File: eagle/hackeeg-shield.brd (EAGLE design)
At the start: 101.6 x 53.3 mm, 144 parts, among them IC1 ADS1299IPAG, IC10 TXB0108PWR, IC11 TXB0108PWR, IC2 TPS72325DBVT, IC3 TPS73225DBVT, IC5 24AA256UID, IC6 TPS60403DBVT, IC7 OPA376DBV, IC8 OPA376DBV, IC9 TXS0102DCUR

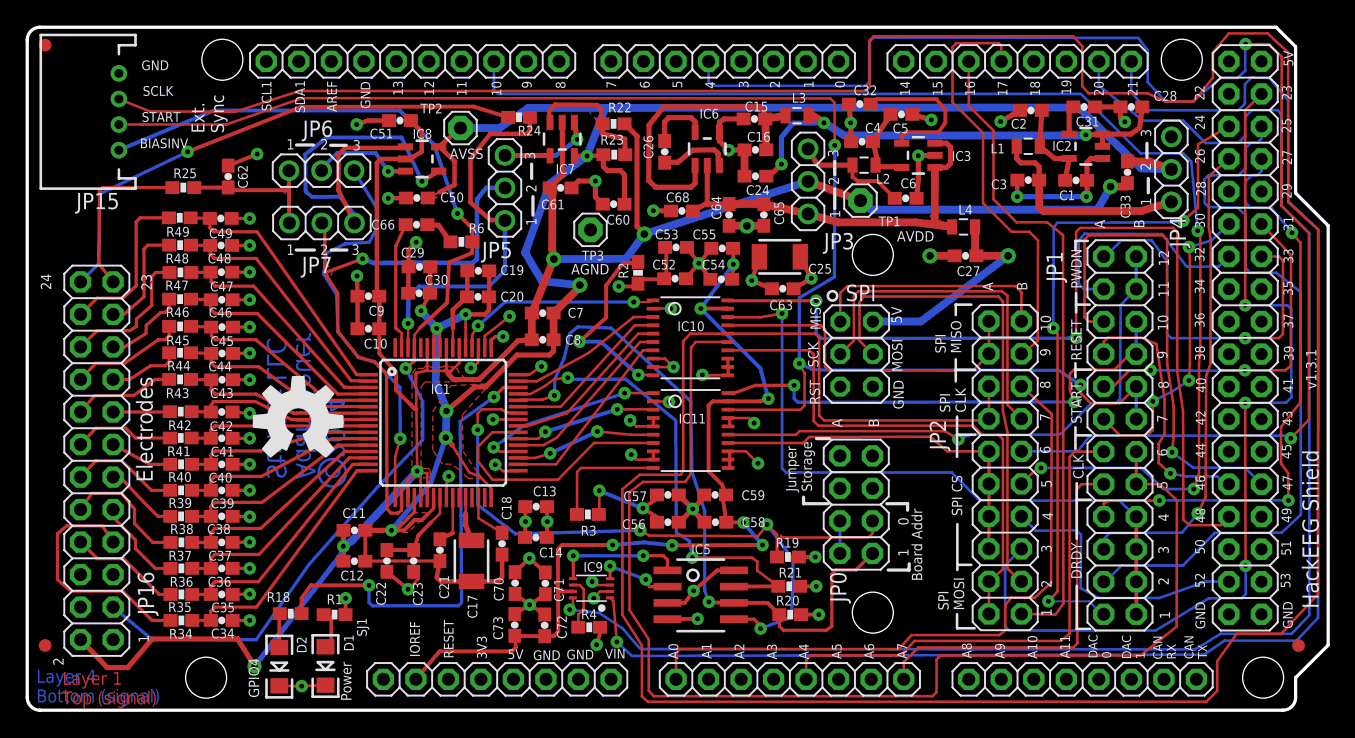
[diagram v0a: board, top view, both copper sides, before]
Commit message: fixed schematic and board bug - opamp OPA376 VDD and VSS pins were reversed; updated schematic and board version to 1.3.1
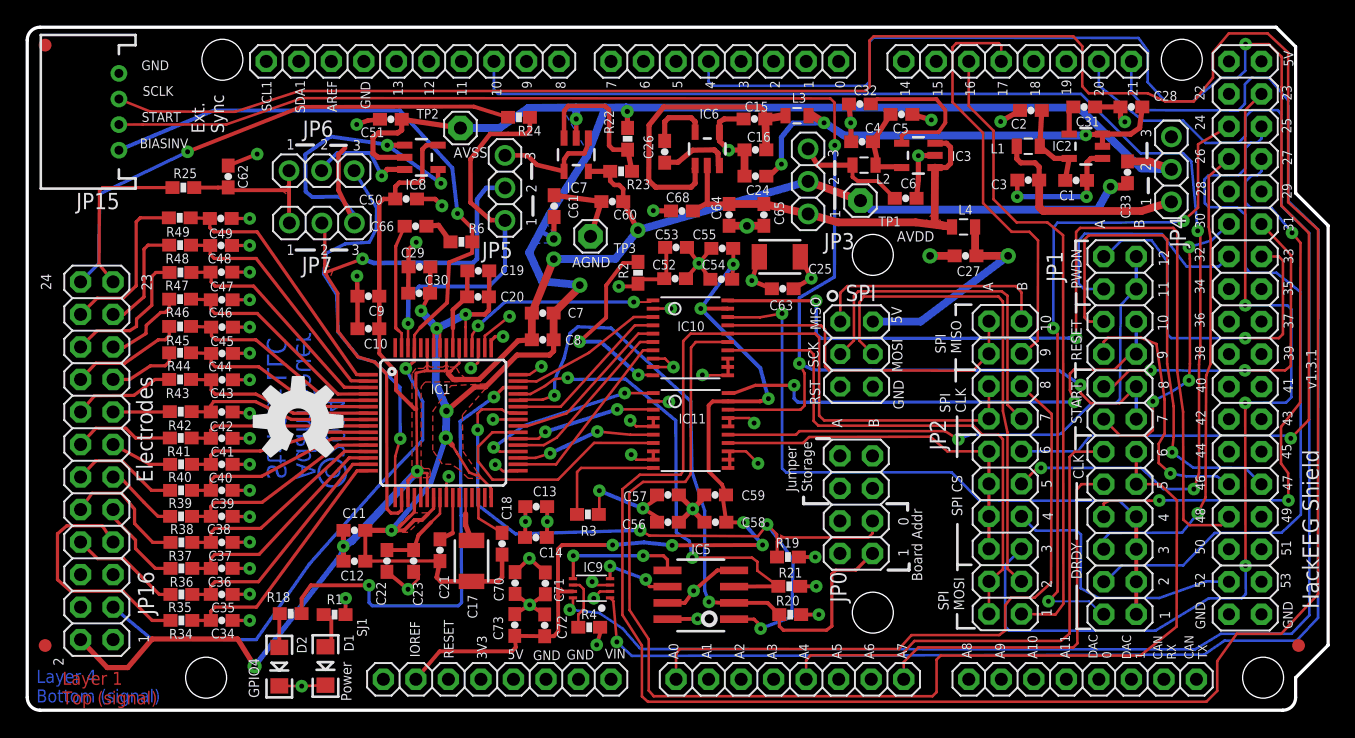
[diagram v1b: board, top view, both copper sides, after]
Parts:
- moved IC7 1.64 mm to (43.0, 43.5)
- moved R22 1.60 mm to (47.0, 44.8), turned to 90 degrees
- moved C61 1.51 mm to (41.3, 39.5), turned to 270 degrees
- moved R23 1.40 mm to (46.5, 42.2)
- moved C50 0.84 mm to (29.7, 40.1), turned to 0 degrees
- moved C51 0.72 mm to (28.5, 46.3)
- moved TP3 0.51 mm to (44.1, 37.1)
- moved C60 0.23 mm to (45.8, 39.9)
- moved C66 0.15 mm to (30.5, 37.9)
- moved IC8 0.14 mm to (30.9, 43.3)
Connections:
- net AVDD: now also C50.1, C60.1, IC7.5, IC8.5, R23.1; no longer C51.2, C61.2, IC7.2, IC8.2, R22.2
- net AVSS: now also C51.2, C61.2, IC7.2, IC8.2, R22.2; no longer C50.1, C60.1, IC7.5, IC8.5, R23.1
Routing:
- net AVDD: track 175.6 -> 160.1 mm
- net N$17: track 32.7 -> 29.2 mm, vias 1 -> 2
- net DVDD: track 42.1 -> 39.5 mm
- net AGND: track 152.4 -> 154.6 mm, vias 56 -> 55
- net N$18: track 10.9 -> 9.01 mm, vias 1 -> 0
- net N$15: track 10.3 -> 12.0 mm
- net AVSS: track 183.1 -> 184.1 mm, vias 8 -> 10
- net N$16: track 7.95 -> 8.49 mm

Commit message: improved AVSS trace width on bottom layer; removed trace running through the middle of caps; improved text sizes for configuration labels
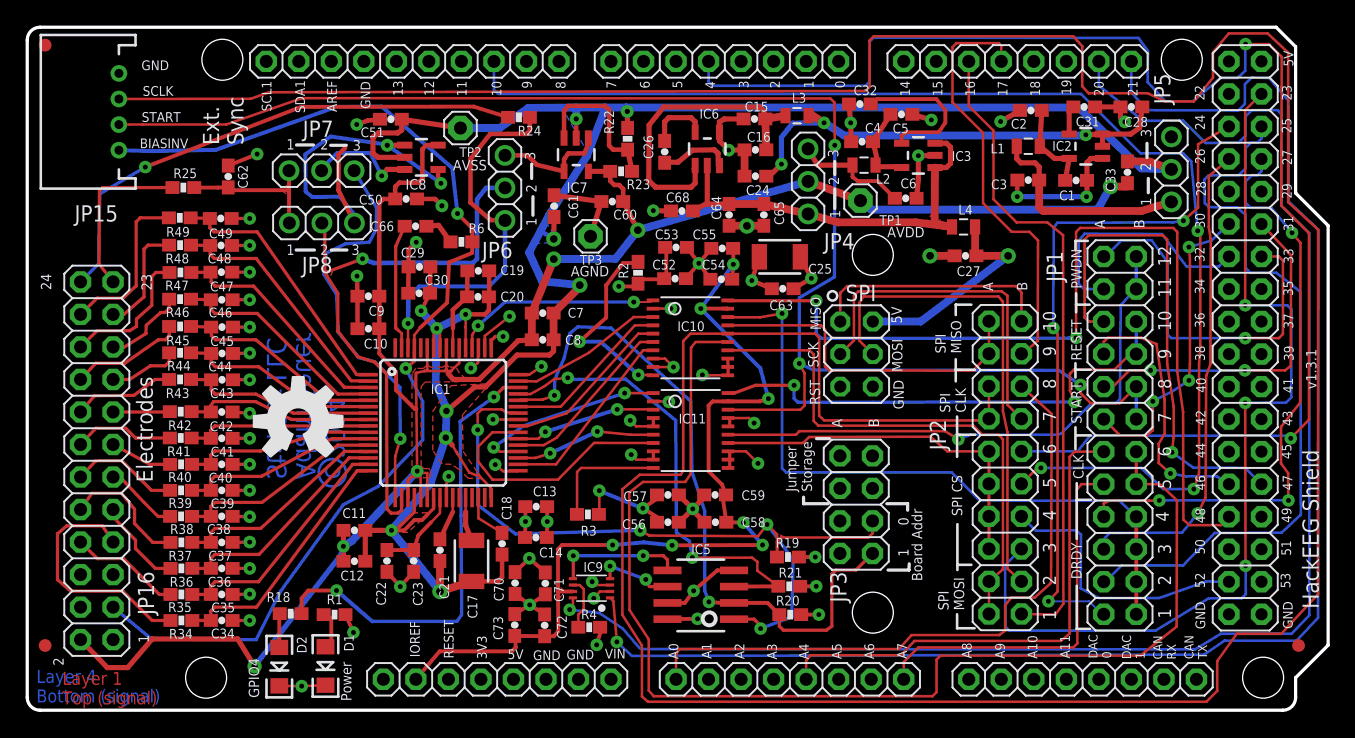
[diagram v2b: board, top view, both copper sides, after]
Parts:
- removed JP0: BOARD_ADDRESS, headers:2X04
- added JP20: PWMH, SmartPrj:1X10
- JP3: value 5V-2.5V -> BOARD_ADDRESS; device headers:1X03 -> headers:2X04
- JP4: value -2.5V-GND -> 5V-2.5V
- JP5: value SRB1-BIAS -> -2.5V-GND; device adafruit:1X03 -> headers:1X03
- JP6: value SRB2-REF_ELEC -> SRB1-BIAS
- JP7: value SRB1-REF_ELEC -> SRB2-REF_ELEC
- JP8: value PWMH -> SRB1-REF_ELEC; device SmartPrj:1X10 -> adafruit:1X03
- moved JP5 52.1 mm to (89.5, 42.4)
- moved JP4 28.4 mm to (61.1, 41.4)
- moved JP3 25.5 mm to (64.9, 16.2)
- moved JP8 14.5 mm to (23.1, 38.2)
- moved JP6 14.4 mm to (37.4, 40.9), turned to 90 degrees
- moved JP7 4.09 mm to (23.1, 42.3)
- renumbered JP10 to JP22, JP11 to JP23, JP12 to JP24, JP13 to JP25, JP14 to JP26, JP9 to JP21
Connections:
- net !ADC_CS_1: now also JP20.8; no longer JP8.8
- net +2.5V: now also JP4.3; no longer JP3.3
- net -2.5V: now also JP5.1; no longer JP4.1
- net AGND: now also JP5.3; no longer JP4.3
- net AVDD: now also JP4.2; no longer JP3.2
- net AVSS: now also JP5.2; no longer JP4.2
- net BIAS_ELEC: now also JP6.1; no longer JP5.1
- net BOARD_ADDR_0: now also JP3.3; no longer JP0.3
- net BOARD_ADDR_1: now also JP3.1; no longer JP0.1
- net DVDD: now also JP3.2, JP3.4; no longer JP0.2, JP0.4
- net N$16: now also JP7.2; no longer JP6.2
- net N$17: now also JP8.3; no longer JP7.3
- net N$18: now also JP6.3; no longer JP5.3
- net N$27: now also JP20.3; no longer JP8.3
- net N$28: now also JP20.4; no longer JP8.4
- net N$29: now also JP20.5; no longer JP8.5
- net N$30: now also JP20.6; no longer JP8.6
- net N$31: now also JP20.7; no longer JP8.7
- net N$33: now also JP20.10; no longer JP8.10
- net N$6: now also JP20.9; no longer JP8.9
- net N$6001: now also JP20.2; no longer JP8.2
- net N$6002: now also JP20.1; no longer JP8.1
- net REF_ELEC: now also JP8.1; no longer JP6.1
- net SRB1: now also JP6.2, JP8.2; no longer JP5.2, JP7.2
- net SRB2: now also JP7.3; no longer JP6.3
- net VCC_5V_FILTERED: now also JP4.1; no longer JP3.1
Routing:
- net AVSS: track 184.1 -> 185.2 mm, vias 10 -> 11
- net AGND: track 154.6 -> 153.7 mm
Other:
- board text removed: "SJ1"

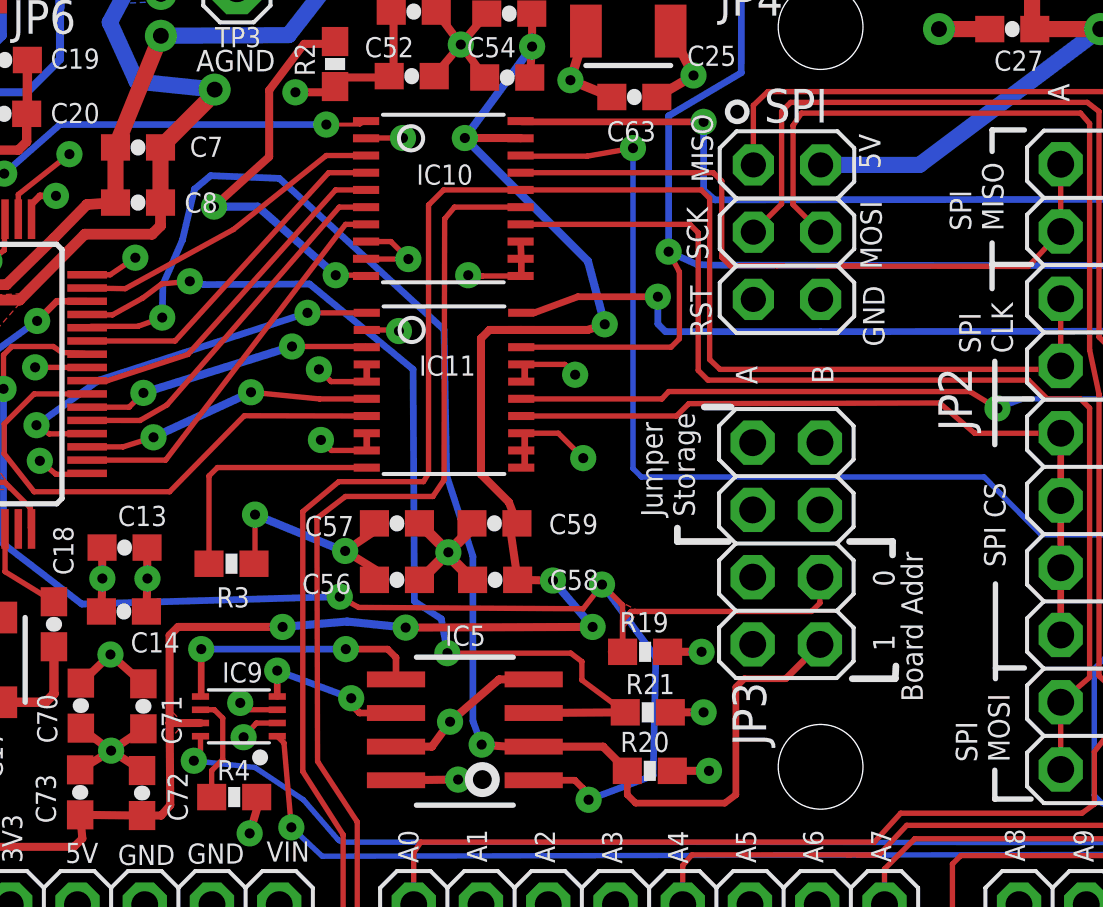
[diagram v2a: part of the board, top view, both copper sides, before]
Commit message: improved trace routing on bottom layer
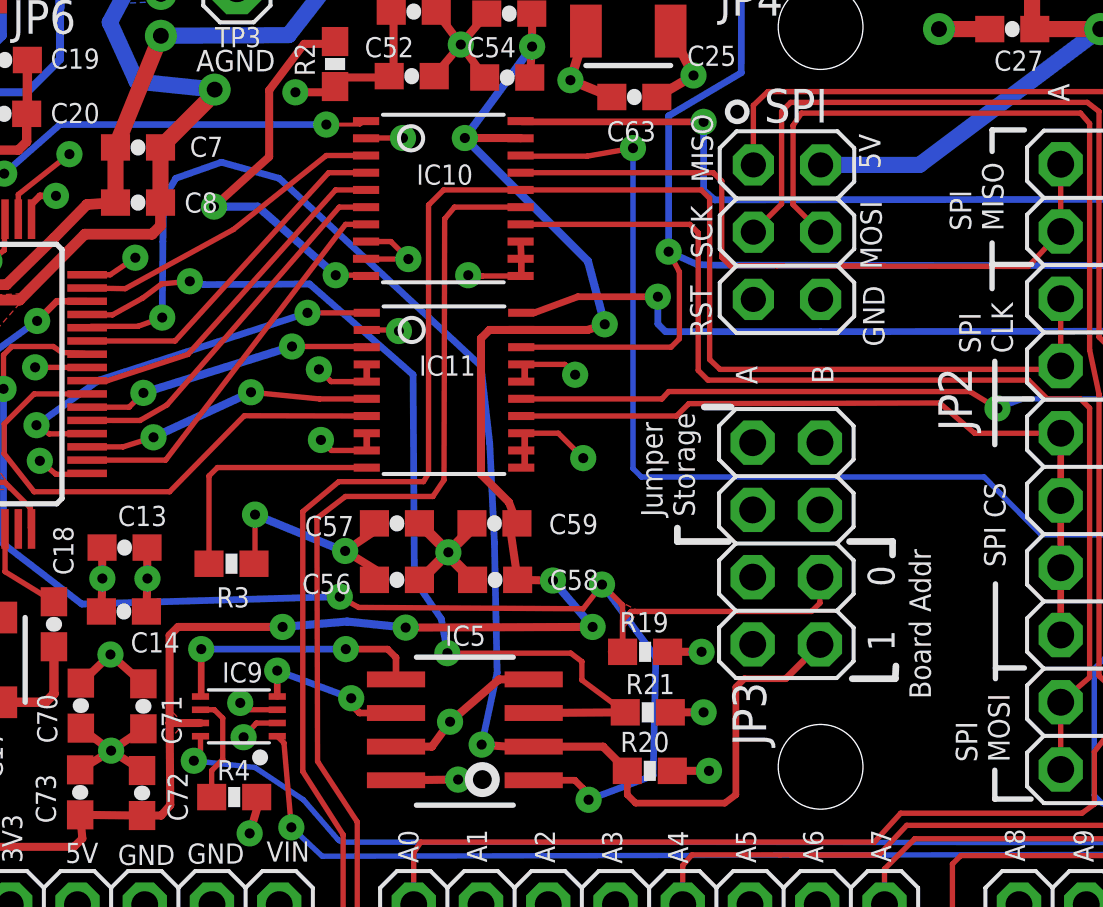
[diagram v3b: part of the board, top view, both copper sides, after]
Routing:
- net BOARD_ADDR_1: track 54.8 -> 56.2 mm
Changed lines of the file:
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@@
 <grid distance="4" unitdist="mil" unit="mil" style="lines" multiple="1" display="no" altdistance="0.001" altunitdist="inch" altunit="inch"/>
 <layers>
-<layer number="1" name="Top" color="4" fill="1" visible="yes" active="yes"/>
+<layer number="1" name="Top" color="4" fill="1" visible="no" active="yes"/>
 <layer number="2" name="AGND" color="3" fill="1" visible="no" active="yes"/>
 <layer number="3" name="Route3" color="4" fill="3" visible="no" active="no"/>
@@
 <hole x="66.167" y="35.687" drill="3.2"/>
 <hole x="66.167" y="7.747" drill="3.2"/>
-<text x="70.0278" y="10.2108" size="0.8128" layer="21" font="vector" ratio="12" rot="R90">Board Addr</text>
-<text x="68.961" y="14.5542" size="0.8128" layer="21" font="vector" ratio="12" rot="R90">0</text>
-<text x="68.961" y="12.1158" size="0.8128" layer="21" font="vector" ratio="12" rot="R90">1</text>
+<text x="70.3326" y="10.3124" size="0.8128" layer="21" font="vector" ratio="12" rot="R90">Board Addr</text>
+<text x="68.961" y="14.5542" size="1.016" layer="21" font="vector" ratio="12" rot="R90">0</text>
+<text x="68.961" y="12.1158" size="1.016" layer="21" font="vector" ratio="12" rot="R90">1</text>
 <text x="61.4172" y="17.1958" size="0.8128" layer="21" font="vector" ratio="12" rot="R90">Jumper
 Storage</text>
@@
 <text x="68.4276" y="30.3276" size="0.8128" layer="21" font="vector" ratio="12" rot="R90">5V</text>
 <text x="62.103" y="29.8196" size="0.8128" layer="21" font="vector" ratio="12" rot="R90">MISO</text>
-<text x="61.9252" y="26.8986" size="0.8128" layer="21" font="vector" ratio="12" rot="R90">SCK</text>
+<text x="62.0776" y="26.9494" size="0.8128" layer="21" font="vector" ratio="12" rot="R90">SCK</text>
 <text x="62.0522" y="23.9776" size="0.8128" layer="21" font="vector" ratio="12" rot="R90">RST</text>
 <text x="9.144" y="48.1076" size="0.762" layer="21" font="vector" ratio="12">SCLK</text>
@@
 <wire x1="40.386" y1="24.384" x2="38.608" y2="24.384" width="0.2032" layer="1"/>
 <wire x1="41.3004" y1="24.7142" x2="40.386" y2="24.384" width="0.2032" layer="1"/>
-<wire x1="42.5196" y1="29.5656" x2="42.0624" y2="27.6352" width="0.254" layer="16"/>
-<wire x1="42.0624" y1="27.6352" x2="41.3258" y2="25.9588" width="0.254" layer="16"/>
-<wire x1="41.3258" y1="25.9588" x2="41.3004" y2="24.7142" width="0.254" layer="16"/>
-<wire x1="43.1292" y1="30.0736" x2="42.5196" y2="29.5656" width="0.254" layer="16"/>
-<wire x1="45.72" y1="29.972" x2="43.1292" y2="30.0736" width="0.254" layer="16"/>
-<wire x1="51.943" y1="24.257" x2="45.72" y2="29.972" width="0.254" layer="16"/>
-<wire x1="52.0446" y1="18.7452" x2="51.943" y2="24.257" width="0.254" layer="16"/>
-<wire x1="53.0352" y1="15.6972" x2="52.0446" y2="18.7452" width="0.254" layer="16"/>
+<wire x1="41.8084" y1="29.972" x2="41.3512" y2="29.1592" width="0.254" layer="16"/>
+<wire x1="41.3512" y1="29.1592" x2="41.3258" y2="27.5844" width="0.254" layer="16"/>
+<wire x1="41.3258" y1="27.5844" x2="41.3004" y2="24.7142" width="0.254" layer="16"/>
+<wire x1="43.5356" y1="30.5816" x2="41.8084" y2="29.972" width="0.254" layer="16"/>
+<wire x1="45.72" y1="29.972" x2="43.5356" y2="30.5816" width="0.254" layer="16"/>
+<wire x1="53.34" y1="22.8854" x2="45.72" y2="29.972" width="0.254" layer="16"/>
+<wire x1="53.6702" y1="19.9644" x2="53.34" y2="22.8854" width="0.254" layer="16"/>
+<wire x1="53.848" y1="16.2052" x2="53.6702" y2="19.9644" width="0.254" layer="16"/>
 <wire x1="38.608" y1="24.384" x2="38.4636" y2="24.3306" width="0.1524" layer="1"/>
 <via x="41.3004" y="24.7142" extent="1-16" drill="0.381"/>
@@
 <wire x1="55.2542" y1="8.4328" x2="53.3654" y2="8.5852" width="0.3048" layer="1"/>
 <via x="53.3654" y="8.5852" extent="1-16" drill="0.381"/>
-<wire x1="53.3654" y1="8.5852" x2="53.0352" y2="9.4742" width="0.254" layer="16"/>
-<wire x1="53.0352" y1="9.4742" x2="53.0352" y2="15.6972" width="0.254" layer="16"/>
+<wire x1="53.3654" y1="8.5852" x2="53.9496" y2="11.303" width="0.254" layer="16"/>
+<wire x1="53.9496" y1="11.303" x2="53.848" y2="16.2052" width="0.254" layer="16"/>
 <wire x1="55.3304" y1="8.509" x2="57.951" y2="8.509" width="0.3048" layer="1"/>
 <wire x1="57.951" y1="8.509" x2="58.8654" y2="7.5946" width="0.3048" layer="1"/>
@@
 <wire x1="42.8752" y1="25.9588" x2="42.3418" y2="26.0858" width="0.254" layer="16"/>
 <wire x1="46.863" y1="25.9842" x2="42.8752" y2="25.9588" width="0.254" layer="16"/>
-<wire x1="50.7746" y1="22.7584" x2="46.863" y2="25.9842" width="0.254" layer="16"/>
-<wire x1="50.8254" y1="13.9954" x2="50.7746" y2="22.7584" width="0.254" layer="16"/>
+<wire x1="50.7746" y1="22.5552" x2="46.863" y2="25.9842" width="0.254" layer="16"/>
+<wire x1="50.8254" y1="14.8082" x2="50.7746" y2="22.5552" width="0.254" layer="16"/>
 <wire x1="38.481" y1="24.8158" x2="38.4636" y2="24.8306" width="0.1524" layer="1"/>
 <via x="42.3418" y="26.0858" extent="1-16" drill="0.381"/>
 <wire x1="55.3304" y1="9.779" x2="58.7892" y2="9.8044" width="0.3048" layer="1"/>
-<wire x1="50.8254" y1="13.9954" x2="51.8414" y2="13.335" width="0.254" layer="16"/>
+<wire x1="50.8254" y1="14.8082" x2="51.8414" y2="13.335" width="0.254" layer="16"/>
 <wire x1="51.8414" y1="13.335" x2="52.07" y2="12.0396" width="0.254" layer="16"/>
 <via x="52.07" y="12.0396" extent="1-16" drill="0.381"/>
